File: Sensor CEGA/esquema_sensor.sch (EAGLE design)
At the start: 11 parts

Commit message: sensor cega v1, falta rutear las pistas
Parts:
- removed PRO-MINI: ARDUINO-PRO-MINI-3.3V#NP, diy-modules:ARDUINO-PRO-MINI-3.3V#NP
- added U$1: PRO_MINI_CEGA, fablab_uchile:PRO_MINI_CEGA
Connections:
- removed net N$2: PRO-MINI.A4, RTC.4
- removed net N$9: PRO-MINI.A5, RTC.3
- new net A4: RTC.4, U$1.A4
- new net A5: RTC.3, U$1.A5
- net +5V: now also U$1.VCC
- net GNDA: now also U$1.GND; no longer PRO-MINI.GND.3
- net N$1: now also U$1.*3; no longer PRO-MINI.D3
- net N$10: now also U$1.12; no longer PRO-MINI.D12
- net N$11: now also U$1.*11; no longer PRO-MINI.D11
- net N$12: now also U$1.13; no longer PRO-MINI.D13
- net N$13: now also U$1.*10; no longer PRO-MINI.D10
- net N$3: now also U$1.2; no longer PRO-MINI.D2
- net N$5: now also U$1.RXI; no longer PRO-MINI.D0/RX
- net N$6: now also U$1.TXO; no longer PRO-MINI.D1/TX
- net N$8: now also U$1.*5; no longer PRO-MINI.D5
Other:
- moved on the sheet: MICRO-SD, RTC

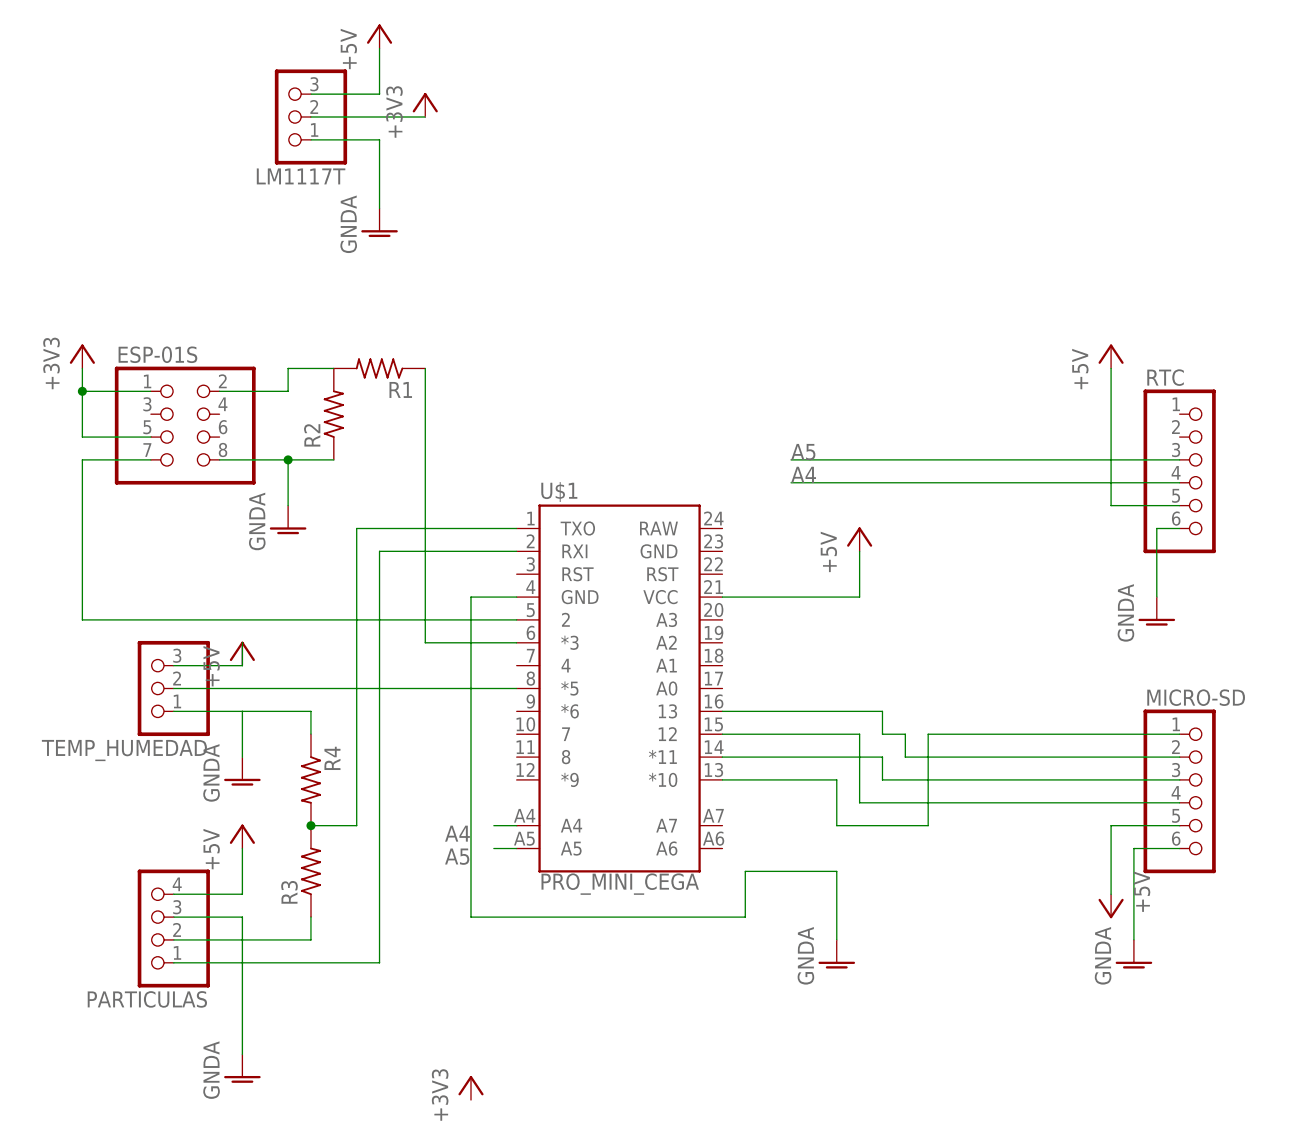
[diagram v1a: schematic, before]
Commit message: versión 1.0 del sensor en PCB
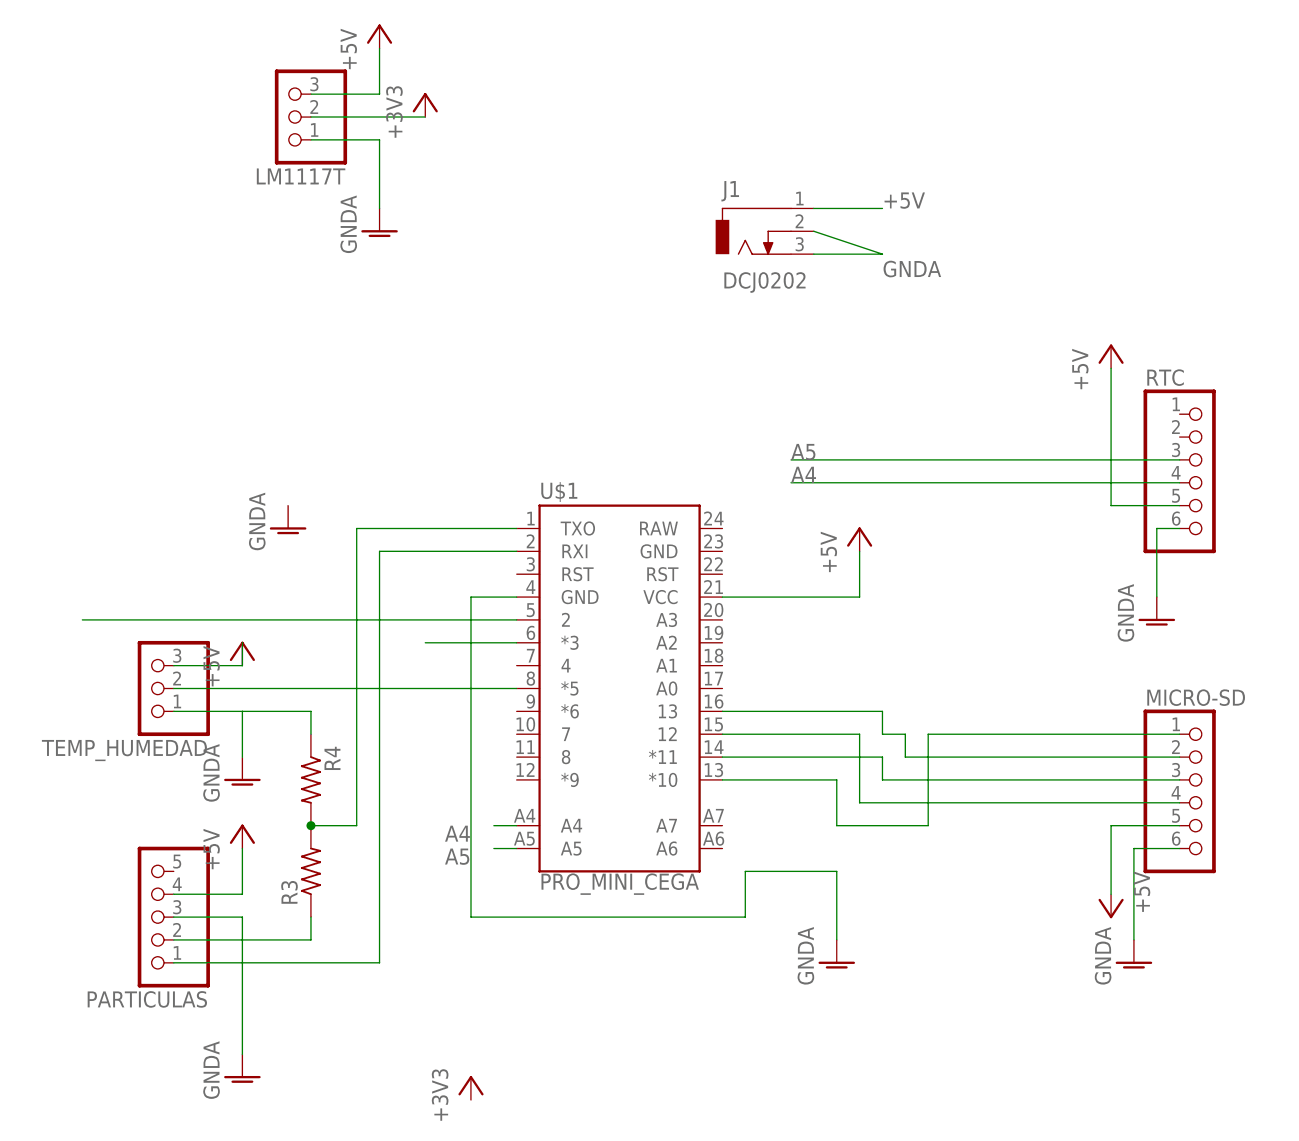
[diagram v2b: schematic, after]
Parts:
- removed ESP-01S: (no value), pinhead:PINHD-2X4
- removed R1, R2: (no value), resistor:R-US_0207/7
- added J1: DCJ0202, con-jack:DCJ0202
- PARTICULAS: device pinhead:PINHD-1X4 -> pinhead:PINHD-1X5
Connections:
- removed net N$4: ESP-01S.2, R1.2, R2.2
- net +3V3: no longer ESP-01S.1, ESP-01S.5
- net +5V: now also J1.1
- net GNDA: now also J1.2, J1.3; no longer ESP-01S.8, R2.1
- net N$1: no longer R1.1
- net N$3: no longer ESP-01S.7
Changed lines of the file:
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@@
 <?xml version="1.0" encoding="utf-8"?>
 <!DOCTYPE eagle SYSTEM "eagle.dtd">
-<eagle version="9.2.1">
+<eagle version="9.4.2">
 <drawing>
 <settings>
@@
 <parts>
 <part name="TEMP_HUMEDAD" library="adafruit" library_urn="urn:adsk.eagle:library:420" deviceset="PINHD-1X3" device=""/>
-<part name="ESP-01S" library="pinhead" library_urn="urn:adsk.eagle:library:325" deviceset="PINHD-2X4" device="" package3d_urn="urn:adsk.eagle:package:22461/2"/>
-<part name="PARTICULAS" library="pinhead" library_urn="urn:adsk.eagle:library:325" deviceset="PINHD-1X4" device="" package3d_urn="urn:adsk.eagle:package:22407/2"/>
+<part name="PARTICULAS" library="pinhead" library_urn="urn:adsk.eagle:library:325" deviceset="PINHD-1X5" device="" package3d_urn="urn:adsk.eagle:package:22469/2"/>
 <part name="+3V1" library="supply1" library_urn="urn:adsk.eagle:library:371" deviceset="+3V3" device=""/>
 <part name="P+1" library="supply1" library_urn="urn:adsk.eagle:library:371" deviceset="+5V" device=""/>
@@
 <part name="RTC" library="adafruit" library_urn="urn:adsk.eagle:library:420" deviceset="PINHD-1X6" device="B"/>
 <part name="MICRO-SD" library="adafruit" library_urn="urn:adsk.eagle:library:420" deviceset="PINHD-1X6" device="B"/>
-<part name="+3V2" library="supply1" library_urn="urn:adsk.eagle:library:371" deviceset="+3V3" device=""/>
 <part name="GND1" library="supply1" library_urn="urn:adsk.eagle:library:371" deviceset="GNDA" device=""/>
 <part name="P+2" library="supply1" library_urn="urn:adsk.eagle:library:371" deviceset="+5V" device=""/>
 <part name="GND3" library="supply1" library_urn="urn:adsk.eagle:library:371" deviceset="GNDA" device=""/>
-<part name="R1" library="resistor" library_urn="urn:adsk.eagle:library:348" deviceset="R-US_" device="0207/7" package3d_urn="urn:adsk.eagle:package:25942/1"/>
-<part name="R2" library="resistor" library_urn="urn:adsk.eagle:library:348" deviceset="R-US_" device="0207/7" package3d_urn="urn:adsk.eagle:package:25942/1"/>
 <part name="P+3" library="supply1" library_urn="urn:adsk.eagle:library:371" deviceset="+5V" device=""/>
 <part name="GND4" library="supply1" library_urn="urn:adsk.eagle:library:371" deviceset="GNDA" device=""/>
@@
 <part name="GND7" library="supply1" library_urn="urn:adsk.eagle:library:371" deviceset="GNDA" device=""/>
 <part name="U$1" library="fablab_uchile" deviceset="PRO_MINI_CEGA" device=""/>
+<part name="J1" library="con-jack" library_urn="urn:adsk.eagle:library:154" deviceset="DCJ0202" device="" package3d_urn="urn:adsk.eagle:package:7491/1"/>
 </parts>
 <sheets>
@@
 <attribute name="VALUE" x="34.29" y="55.88" size="1.778" layer="96" rot="R180"/>
 </instance>
-<instance part="ESP-01S" gate="A" x="30.48" y="76.2" smashed="yes">
-<attribute name="NAME" x="24.13" y="84.455" size="1.778" layer="95"/>
-<attribute name="VALUE" x="24.13" y="68.58" size="1.778" layer="96"/>
-</instance>
 <instance part="PARTICULAS" gate="A" x="27.94" y="22.86" smashed="yes" rot="R180">
 <attribute name="NAME" x="34.29" y="14.605" size="1.778" layer="95" rot="R180"/>
@@
 <attribute name="VALUE" x="138.43" y="25.4" size="1.778" layer="96"/>
 </instance>
-<instance part="+3V2" gate="G$1" x="20.32" y="86.36" smashed="yes">
-<attribute name="VALUE" x="17.78" y="81.28" size="1.778" layer="96" rot="R90"/>
-</instance>
 <instance part="GND1" gate="1" x="43.18" y="66.04" smashed="yes">
 <attribute name="VALUE" x="40.64" y="63.5" size="1.778" layer="96" rot="R90"/>
@@
 <instance part="GND3" gate="1" x="38.1" y="38.1" smashed="yes">
 <attribute name="VALUE" x="35.56" y="35.56" size="1.778" layer="96" rot="R90"/>
-</instance>
-<instance part="R1" gate="G$1" x="53.34" y="83.82" smashed="yes" rot="R180">
-<attribute name="NAME" x="57.15" y="82.3214" size="1.778" layer="95" rot="R180"/>
-<attribute name="VALUE" x="57.15" y="87.122" size="1.778" layer="96" rot="R180"/>
-</instance>
-<instance part="R2" gate="G$1" x="48.26" y="78.74" smashed="yes" rot="R90">
-<attribute name="NAME" x="46.7614" y="74.93" size="1.778" layer="95" rot="R90"/>
-<attribute name="VALUE" x="51.562" y="74.93" size="1.778" layer="96" rot="R90"/>
 </instance>
 <instance part="P+3" gate="1" x="38.1" y="33.02" smashed="yes">
@@
 <attribute name="NAME" x="71.12" y="69.342" size="1.778" layer="95" font="vector"/>
 <attribute name="VALUE" x="71.12" y="27.686" size="1.778" layer="96" font="vector" align="top-left"/>
+</instance>
+<instance part="J1" gate="G$1" x="93.98" y="99.06" smashed="yes">
+<attribute name="NAME" x="91.44" y="102.87" size="1.778" layer="95"/>
+<attribute name="VALUE" x="91.44" y="92.71" size="1.778" layer="96"/>
 </instance>
 </instances>
@@
 <net name="N$3" class="0">
 <segment>
-<pinref part="ESP-01S" gate="A" pin="7"/>
-<wire x1="27.94" y1="73.66" x2="20.32" y2="73.66" width="0.1524" layer="91"/>
-<wire x1="20.32" y1="73.66" x2="20.32" y2="55.88" width="0.1524" layer="91"/>
 <wire x1="20.32" y1="55.88" x2="68.58" y2="55.88" width="0.1524" layer="91"/>
 <pinref part="U$1" gate="G$1" pin="2"/>
@@
 <net name="+3V3" class="0">
 <segment>
-<pinref part="ESP-01S" gate="A" pin="1"/>
-<pinref part="+3V2" gate="G$1" pin="+3V3"/>
-<wire x1="27.94" y1="81.28" x2="20.32" y2="81.28" width="0.1524" layer="91"/>
-<wire x1="20.32" y1="81.28" x2="20.32" y2="83.82" width="0.1524" layer="91"/>
-<pinref part="ESP-01S" gate="A" pin="5"/>
-<wire x1="27.94" y1="76.2" x2="20.32" y2="76.2" width="0.1524" layer="91"/>
-<wire x1="20.32" y1="81.28" x2="20.32" y2="76.2" width="0.1524" layer="91"/>
-<junction x="20.32" y="81.28"/>
-</segment>
-<segment>
 <pinref part="LM1117T" gate="A" pin="2"/>
 <wire x1="45.72" y1="111.76" x2="58.42" y2="111.76" width="0.1524" layer="91"/>
@@
 </net>
 <net name="GNDA" class="0">
-<segment>
-<pinref part="GND1" gate="1" pin="GNDA"/>
-<pinref part="ESP-01S" gate="A" pin="8"/>
-<wire x1="35.56" y1="73.66" x2="43.18" y2="73.66" width="0.1524" layer="91"/>
-<pinref part="R2" gate="G$1" pin="1"/>
-<wire x1="43.18" y1="73.66" x2="48.26" y2="73.66" width="0.1524" layer="91"/>
-<wire x1="43.18" y1="73.66" x2="43.18" y2="68.58" width="0.1524" layer="91"/>
-<junction x="43.18" y="73.66"/>
-</segment>
 <segment>
 <pinref part="TEMP_HUMEDAD" gate="A" pin="1"/>
@@
 <pinref part="GND7" gate="1" pin="GNDA"/>
 </segment>
+<segment>
+<pinref part="J1" gate="G$1" pin="3"/>
+<wire x1="101.6" y1="96.52" x2="109.22" y2="96.52" width="0.1524" layer="91"/>
+<pinref part="J1" gate="G$1" pin="2"/>
+<wire x1="101.6" y1="99.06" x2="109.22" y2="96.52" width="0.1524" layer="91"/>
+<label x="109.22" y="93.98" size="1.778" layer="95"/>
+</segment>
 </net>
 <net name="+5V" class="0">
@@
 <wire x1="106.68" y1="58.42" x2="106.68" y2="63.5" width="0.1524" layer="91"/>
 </segment>
-</net>
-<net name="N$4" class="0">
-<segment>
-<pinref part="R2" gate="G$1" pin="2"/>
-<pinref part="R1" gate="G$1" pin="2"/>
-<pinref part="ESP-01S" gate="A" pin="2"/>
-<wire x1="35.56" y1="81.28" x2="43.18" y2="81.28" width="0.1524" layer="91"/>
-<wire x1="43.18" y1="81.28" x2="43.18" y2="83.82" width="0.1524" layer="91"/>
-<wire x1="43.18" y1="83.82" x2="48.26" y2="83.82" width="0.1524" layer="91"/>
+<segment>
+<pinref part="J1" gate="G$1" pin="1"/>
+<wire x1="101.6" y1="101.6" x2="109.22" y2="101.6" width="0.1524" layer="91"/>
+<label x="109.22" y="101.6" size="1.778" layer="95"/>
 </segment>
 </net>
 <net name="N$1" class="0">
 <segment>
-<pinref part="R1" gate="G$1" pin="1"/>
-<wire x1="58.42" y1="83.82" x2="58.42" y2="53.34" width="0.1524" layer="91"/>
 <pinref part="U$1" gate="G$1" pin="*3"/>
 <wire x1="58.42" y1="53.34" x2="68.58" y2="53.34" width="0.1524" layer="91"/>

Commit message: actualizado sensor cega y usain bot
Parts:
- removed LM1117T: (no value), adafruit:PINHD-1X3
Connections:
- removed net +3V3: LM1117T.2
- removed net N$1: U$1.*3
- removed net N$3: U$1.2
- removed net N$7: PARTICULAS.2, R3.1
- new net N$2: PARTICULAS.2, R3.2, R4.2
- net +5V: no longer LM1117T.3
- net GNDA: no longer LM1117T.1
- net N$6: now also R3.1; no longer R3.2, R4.2
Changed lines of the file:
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@@
 <part name="TEMP_HUMEDAD" library="adafruit" library_urn="urn:adsk.eagle:library:420" deviceset="PINHD-1X3" device=""/>
 <part name="PARTICULAS" library="pinhead" library_urn="urn:adsk.eagle:library:325" deviceset="PINHD-1X5" device="" package3d_urn="urn:adsk.eagle:package:22469/2"/>
-<part name="+3V1" library="supply1" library_urn="urn:adsk.eagle:library:371" deviceset="+3V3" device=""/>
 <part name="P+1" library="supply1" library_urn="urn:adsk.eagle:library:371" deviceset="+5V" device=""/>
 <part name="GND2" library="supply1" library_urn="urn:adsk.eagle:library:371" deviceset="GNDA" device=""/>
 <part name="RTC" library="adafruit" library_urn="urn:adsk.eagle:library:420" deviceset="PINHD-1X6" device="B"/>
 <part name="MICRO-SD" library="adafruit" library_urn="urn:adsk.eagle:library:420" deviceset="PINHD-1X6" device="B"/>
-<part name="GND1" library="supply1" library_urn="urn:adsk.eagle:library:371" deviceset="GNDA" device=""/>
 <part name="P+2" library="supply1" library_urn="urn:adsk.eagle:library:371" deviceset="+5V" device=""/>
 <part name="GND3" library="supply1" library_urn="urn:adsk.eagle:library:371" deviceset="GNDA" device=""/>
@@
 <part name="GND6" library="supply1" library_urn="urn:adsk.eagle:library:371" deviceset="GNDA" device=""/>
 <part name="P+5" library="supply1" library_urn="urn:adsk.eagle:library:371" deviceset="+5V" device=""/>
-<part name="LM1117T" library="adafruit" library_urn="urn:adsk.eagle:library:420" deviceset="PINHD-1X3" device=""/>
-<part name="P+6" library="supply1" library_urn="urn:adsk.eagle:library:371" deviceset="+5V" device=""/>
-<part name="+3V3" library="supply1" library_urn="urn:adsk.eagle:library:371" deviceset="+3V3" device=""/>
-<part name="GND7" library="supply1" library_urn="urn:adsk.eagle:library:371" deviceset="GNDA" device=""/>
 <part name="U$1" library="fablab_uchile" deviceset="PRO_MINI_CEGA" device=""/>
 <part name="J1" library="con-jack" library_urn="urn:adsk.eagle:library:154" deviceset="DCJ0202" device="" package3d_urn="urn:adsk.eagle:package:7491/1"/>
@@
 <attribute name="VALUE" x="34.29" y="30.48" size="1.778" layer="96" rot="R180"/>
 </instance>
-<instance part="+3V1" gate="G$1" x="63.5" y="5.08" smashed="yes">
-<attribute name="VALUE" x="60.96" y="0" size="1.778" layer="96" rot="R90"/>
-</instance>
 <instance part="P+1" gate="1" x="106.68" y="66.04" smashed="yes">
 <attribute name="VALUE" x="104.14" y="60.96" size="1.778" layer="96" rot="R90"/>
@@
 <attribute name="VALUE" x="138.43" y="25.4" size="1.778" layer="96"/>
 </instance>
-<instance part="GND1" gate="1" x="43.18" y="66.04" smashed="yes">
-<attribute name="VALUE" x="40.64" y="63.5" size="1.778" layer="96" rot="R90"/>
-</instance>
 <instance part="P+2" gate="1" x="38.1" y="53.34" smashed="yes">
 <attribute name="VALUE" x="35.56" y="48.26" size="1.778" layer="96" rot="R90"/>
@@
 <instance part="P+5" gate="1" x="134.62" y="22.86" smashed="yes" rot="R180">
 <attribute name="VALUE" x="137.16" y="27.94" size="1.778" layer="96" rot="R270"/>
-</instance>
-<instance part="LM1117T" gate="A" x="43.18" y="111.76" smashed="yes" rot="R180">
-<attribute name="NAME" x="49.53" y="106.045" size="1.778" layer="95" rot="R180"/>
-<attribute name="VALUE" x="49.53" y="119.38" size="1.778" layer="96" rot="R180"/>
-</instance>
-<instance part="P+6" gate="1" x="53.34" y="121.92" smashed="yes">
-<attribute name="VALUE" x="50.8" y="116.84" size="1.778" layer="96" rot="R90"/>
-</instance>
-<instance part="+3V3" gate="G$1" x="58.42" y="114.3" smashed="yes">
-<attribute name="VALUE" x="55.88" y="109.22" size="1.778" layer="96" rot="R90"/>
-</instance>
-<instance part="GND7" gate="1" x="53.34" y="99.06" smashed="yes">
-<attribute name="VALUE" x="50.8" y="96.52" size="1.778" layer="96" rot="R90"/>
 </instance>
 <instance part="U$1" gate="G$1" x="78.74" y="48.26" smashed="yes">
@@
 </busses>
 <nets>
-<net name="N$3" class="0">
-<segment>
-<wire x1="20.32" y1="55.88" x2="68.58" y2="55.88" width="0.1524" layer="91"/>
-<pinref part="U$1" gate="G$1" pin="2"/>
-</segment>
-</net>
 <net name="N$8" class="0">
 <segment>
@@
 <wire x1="30.48" y1="48.26" x2="68.58" y2="48.26" width="0.1524" layer="91"/>
 <pinref part="U$1" gate="G$1" pin="*5"/>
-</segment>
-</net>
-<net name="+3V3" class="0">
-<segment>
-<pinref part="LM1117T" gate="A" pin="2"/>
-<wire x1="45.72" y1="111.76" x2="58.42" y2="111.76" width="0.1524" layer="91"/>
-<pinref part="+3V3" gate="G$1" pin="+3V3"/>
 </segment>
 </net>
@@
 </segment>
 <segment>
-<pinref part="LM1117T" gate="A" pin="1"/>
-<wire x1="45.72" y1="109.22" x2="53.34" y2="109.22" width="0.1524" layer="91"/>
-<wire x1="53.34" y1="109.22" x2="53.34" y2="101.6" width="0.1524" layer="91"/>
-<pinref part="GND7" gate="1" pin="GNDA"/>
-</segment>
-<segment>
 <pinref part="J1" gate="G$1" pin="3"/>
 <wire x1="101.6" y1="96.52" x2="109.22" y2="96.52" width="0.1524" layer="91"/>
@@
 </segment>
 <segment>
-<pinref part="LM1117T" gate="A" pin="3"/>
-<wire x1="45.72" y1="114.3" x2="53.34" y2="114.3" width="0.1524" layer="91"/>
-<wire x1="53.34" y1="114.3" x2="53.34" y2="119.38" width="0.1524" layer="91"/>
-<pinref part="P+6" gate="1" pin="+5V"/>
-</segment>
-<segment>
 <pinref part="U$1" gate="G$1" pin="VCC"/>
 <pinref part="P+1" gate="1" pin="+5V"/>
@@
 <wire x1="101.6" y1="101.6" x2="109.22" y2="101.6" width="0.1524" layer="91"/>
 <label x="109.22" y="101.6" size="1.778" layer="95"/>
-</segment>
-</net>
-<net name="N$1" class="0">
-<segment>
-<pinref part="U$1" gate="G$1" pin="*3"/>
-<wire x1="58.42" y1="53.34" x2="68.58" y2="53.34" width="0.1524" layer="91"/>
 </segment>
 </net>
@@
 <net name="N$6" class="0">
 <segment>
-<pinref part="R3" gate="G$1" pin="2"/>
-<pinref part="R4" gate="G$1" pin="2"/>
-<wire x1="45.72" y1="33.02" x2="50.8" y2="33.02" width="0.1524" layer="91"/>
-<wire x1="50.8" y1="33.02" x2="50.8" y2="66.04" width="0.1524" layer="91"/>
+<wire x1="50.8" y1="22.86" x2="50.8" y2="66.04" width="0.1524" layer="91"/>
 <wire x1="50.8" y1="66.04" x2="68.58" y2="66.04" width="0.1524" layer="91"/>
-<junction x="45.72" y="33.02"/>
 <pinref part="U$1" gate="G$1" pin="TXO"/>
-</segment>
-</net>
-<net name="N$7" class="0">
-<segment>
 <pinref part="R3" gate="G$1" pin="1"/>
-<wire x1="45.72" y1="20.32" x2="45.72" y2="22.86" width="0.1524" layer="91"/>
-<pinref part="PARTICULAS" gate="A" pin="2"/>
-<wire x1="30.48" y1="20.32" x2="45.72" y2="20.32" width="0.1524" layer="91"/>
+<wire x1="50.8" y1="22.86" x2="45.72" y2="22.86" width="0.1524" layer="91"/>
 </segment>
 </net>
@@
 </segment>
 </net>
+<net name="N$2" class="0">
+<segment>
+<pinref part="R3" gate="G$1" pin="2"/>
+<pinref part="R4" gate="G$1" pin="2"/>
+<wire x1="45.72" y1="33.02" x2="43.18" y2="33.02" width="0.1524" layer="91"/>
+<junction x="45.72" y="33.02"/>
+<wire x1="43.18" y1="33.02" x2="43.18" y2="20.32" width="0.1524" layer="91"/>
+<pinref part="PARTICULAS" gate="A" pin="2"/>
+<wire x1="43.18" y1="20.32" x2="30.48" y2="20.32" width="0.1524" layer="91"/>
+</segment>
+</net>
